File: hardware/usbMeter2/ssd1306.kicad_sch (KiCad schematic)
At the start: 9 parts

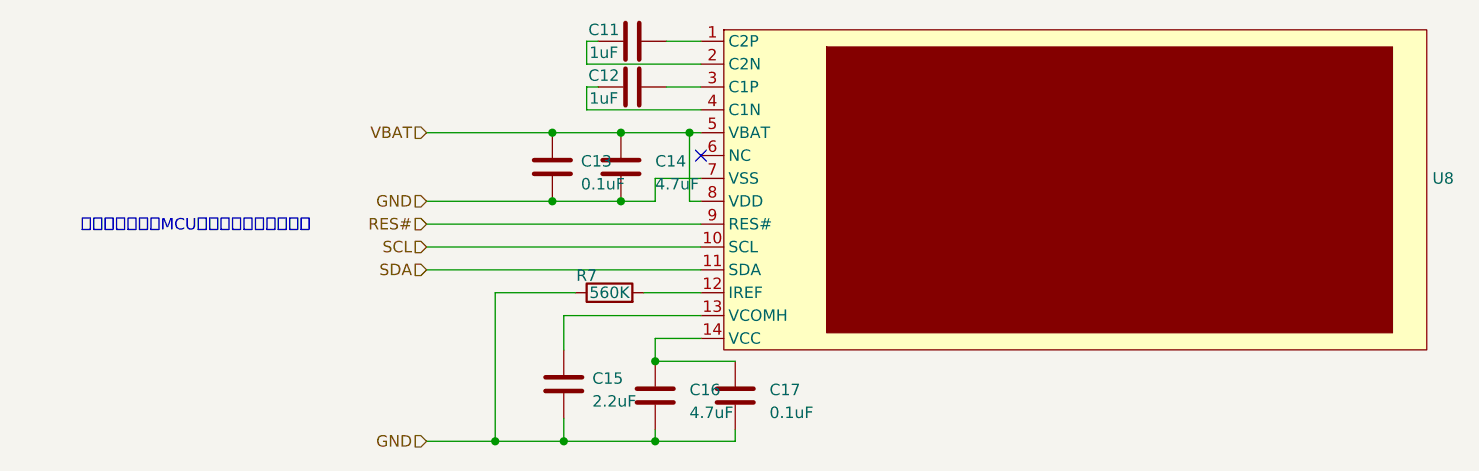
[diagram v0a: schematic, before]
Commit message: usbmeter2尝试缩减了本体的尺寸，采用dcdc+ldo供电避免typea可能存在的高压输入
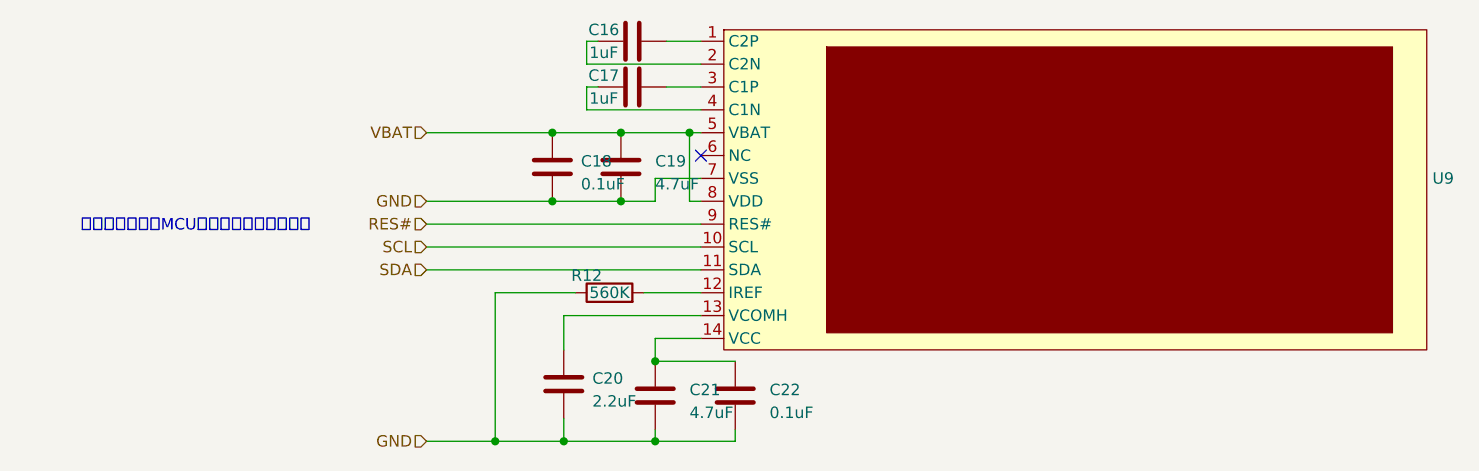
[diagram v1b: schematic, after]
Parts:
- renumbered C11 to C16, C12 to C17, C13 to C18, C14 to C19, C15 to C20, C16 to C21, C17 to C22, R7 to R12, U8 to U9
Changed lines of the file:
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@@
 		(on_board yes)
 		(dnp no)
-		(property "Reference" "C12"
+		(property "Reference" "C17"
 			(at 126.365 87.63 90)
 			(effects
@@
 			(project "usbMeter"
 				(path "/6dddc248-0757-418f-9598-3c64442fd914/0fa69f8f-e323-491c-8eaf-51ac28ff00d5"
-					(reference "C12")
+					(reference "C17")
 					(unit 1)
 				)
@@
 		(on_board yes)
 		(dnp no)
-		(property "Reference" "C11"
+		(property "Reference" "C16"
 			(at 126.365 82.55 90)
 			(effects
@@
 			(project "usbMeter"
 				(path "/6dddc248-0757-418f-9598-3c64442fd914/0fa69f8f-e323-491c-8eaf-51ac28ff00d5"
-					(reference "C11")
+					(reference "C16")
 					(unit 1)
 				)
@@
 		(dnp no)
 		(fields_autoplaced yes)
-		(property "Reference" "U8"
+		(property "Reference" "U9"
 			(at 218.44 99.0599 0)
 			(effects
@@
 			(project "usbMeter"
 				(path "/6dddc248-0757-418f-9598-3c64442fd914/0fa69f8f-e323-491c-8eaf-51ac28ff00d5"
-					(reference "U8")
+					(reference "U9")
 					(unit 1)
 				)
@@
 		(dnp no)
 		(fields_autoplaced yes)
-		(property "Reference" "C16"
+		(property "Reference" "C21"
 			(at 135.89 122.555 0)
 			(effects
@@
 			(project "usbMeter"
 				(path "/6dddc248-0757-418f-9598-3c64442fd914/0fa69f8f-e323-491c-8eaf-51ac28ff00d5"
-					(reference "C16")
+					(reference "C21")
 					(unit 1)
 				)
@@
 		(dnp no)
 		(fields_autoplaced yes)
-		(property "Reference" "C14"
+		(property "Reference" "C19"
 			(at 132.08 97.155 0)
 			(effects
@@
 			(project "usbMeter"
 				(path "/6dddc248-0757-418f-9598-3c64442fd914/0fa69f8f-e323-491c-8eaf-51ac28ff00d5"
-					(reference "C14")
+					(reference "C19")
 					(unit 1)
 				)
@@
 		(dnp no)
 		(fields_autoplaced yes)
-		(property "Reference" "C15"
+		(property "Reference" "C20"
 			(at 125.095 121.285 0)
 			(effects
@@
 			(project "usbMeter"
 				(path "/6dddc248-0757-418f-9598-3c64442fd914/0fa69f8f-e323-491c-8eaf-51ac28ff00d5"
-					(reference "C15")
+					(reference "C20")
 					(unit 1)
 				)
@@
 		(dnp no)
 		(fields_autoplaced yes)
-		(property "Reference" "C13"
+		(property "Reference" "C18"
 			(at 123.825 97.155 0)
 			(effects
@@
 			(project "usbMeter"
 				(path "/6dddc248-0757-418f-9598-3c64442fd914/0fa69f8f-e323-491c-8eaf-51ac28ff00d5"
-					(reference "C13")
+					(reference "C18")
 					(unit 1)
 				)
@@
 		(dnp no)
 		(fields_autoplaced yes)
-		(property "Reference" "C17"
+		(property "Reference" "C22"
 			(at 144.78 122.555 0)
 			(effects
@@
 			(project "usbMeter"
 				(path "/6dddc248-0757-418f-9598-3c64442fd914/0fa69f8f-e323-491c-8eaf-51ac28ff00d5"
-					(reference "C17")
+					(reference "C22")
 					(unit 1)
 				)
@@
 		(on_board yes)
 		(dnp no)
-		(property "Reference" "R7"
+		(property "Reference" "R12"
 			(at 124.46 109.855 90)
 			(effects
@@
 			(project "usbMeter"
 				(path "/6dddc248-0757-418f-9598-3c64442fd914/0fa69f8f-e323-491c-8eaf-51ac28ff00d5"
-					(reference "R7")
+					(reference "R12")
 					(unit 1)
 				)
